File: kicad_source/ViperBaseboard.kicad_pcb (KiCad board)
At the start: 2 copper layers, 100 x 100 mm, 9 parts, among them CN1 ARDUINO_MKR, U1 VL53L0X, U2 VL53L0X, U3 VL53L0X, U4 VL53L0X

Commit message: updated layout, added step of baseboard
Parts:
- added U5: ublox_SAM-M8Q, RF_GPS:ublox_SAM-M8Q, B.Cu at (88.0, 87.0)
- added U6: BNO085, LGA:LGA-28-5832, F.Cu at (128.0, 87.0)
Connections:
- CN1 pad 22: (no net) -> SER_RX
- CN1 pad 23: (no net) -> SER_TX

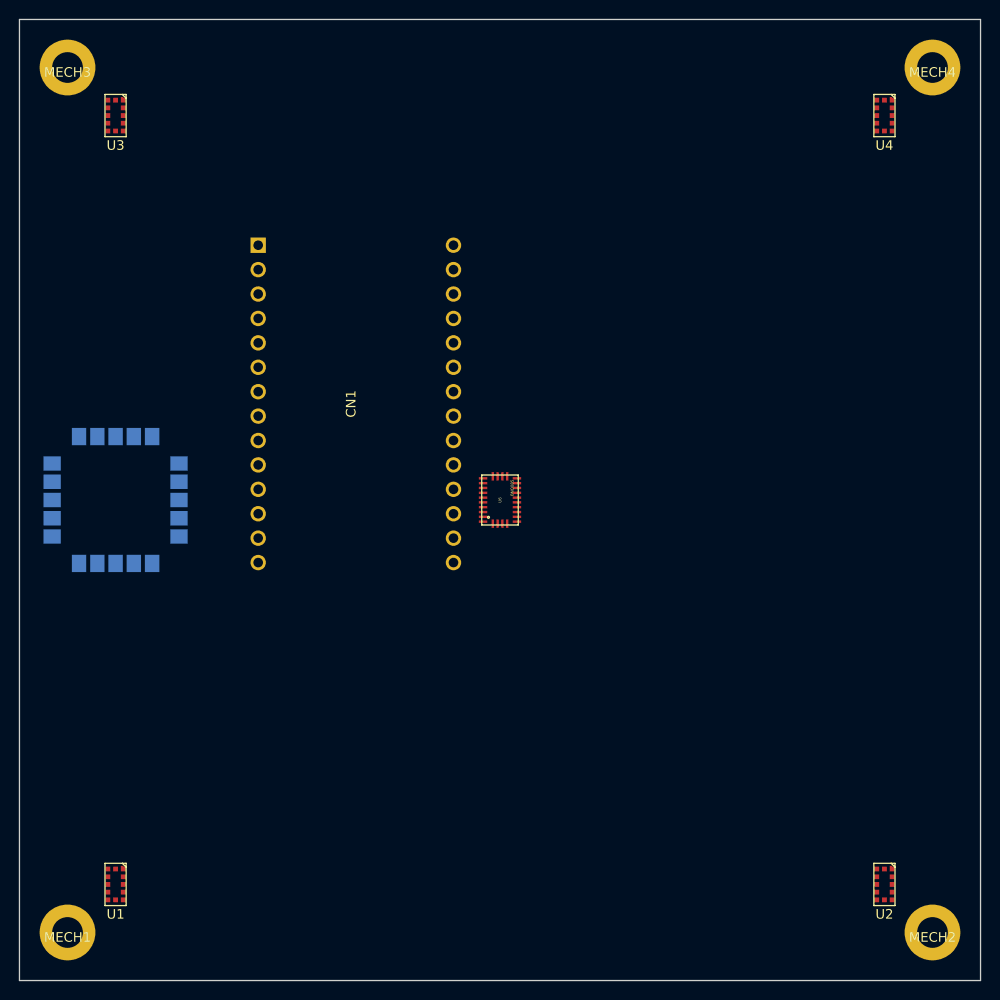
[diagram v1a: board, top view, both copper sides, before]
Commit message: redefined shape of PCB
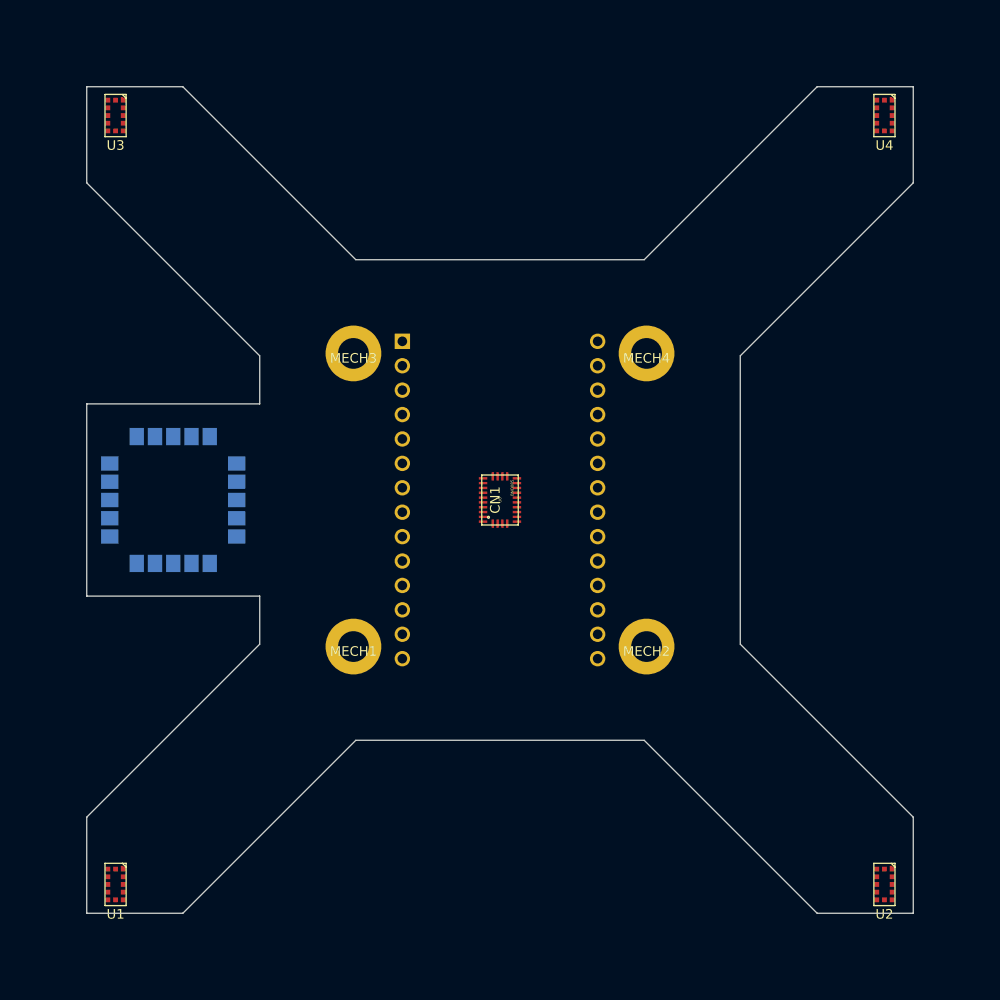
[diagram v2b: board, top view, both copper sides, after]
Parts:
- CN1: footprint MODULE_compute:ARDUINO_MKR -> MODULE_compute:ARDUINO_MKR_BASEBOARD
- moved MECH1 42.1 mm to (112.8, 102.2)
- moved MECH2 42.1 mm to (143.2, 102.2)
- moved MECH3 42.1 mm to (112.8, 71.8)
- moved MECH4 42.1 mm to (143.2, 71.8)
- moved CN1 18.0 mm to (128.0, 87.0)
- moved U5 6.00 mm to (94.0, 87.0)
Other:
- board size 100 x 100 mm -> 86 x 86 mm

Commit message: added BMP388
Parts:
- added C1: 100nF, capacitors:C_0603, F.Cu at (125.5, 78.2)
- added C2: 100nF, capacitors:C_0603, F.Cu at (125.5, 80.7)
- added U7: BMP388, IC_sensor:BMP388, F.Cu at (129.3, 78.7)

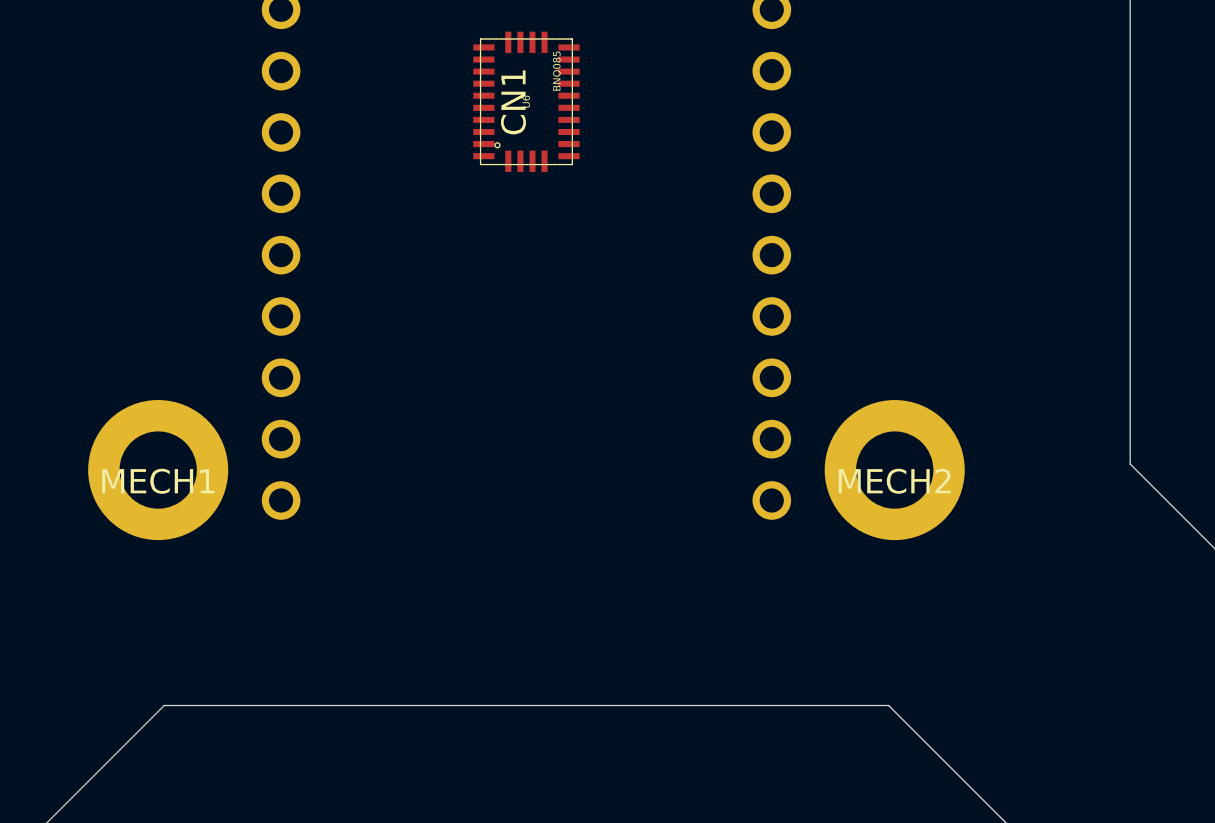
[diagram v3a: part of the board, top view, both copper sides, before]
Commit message: added schematic sheet with MCP2515
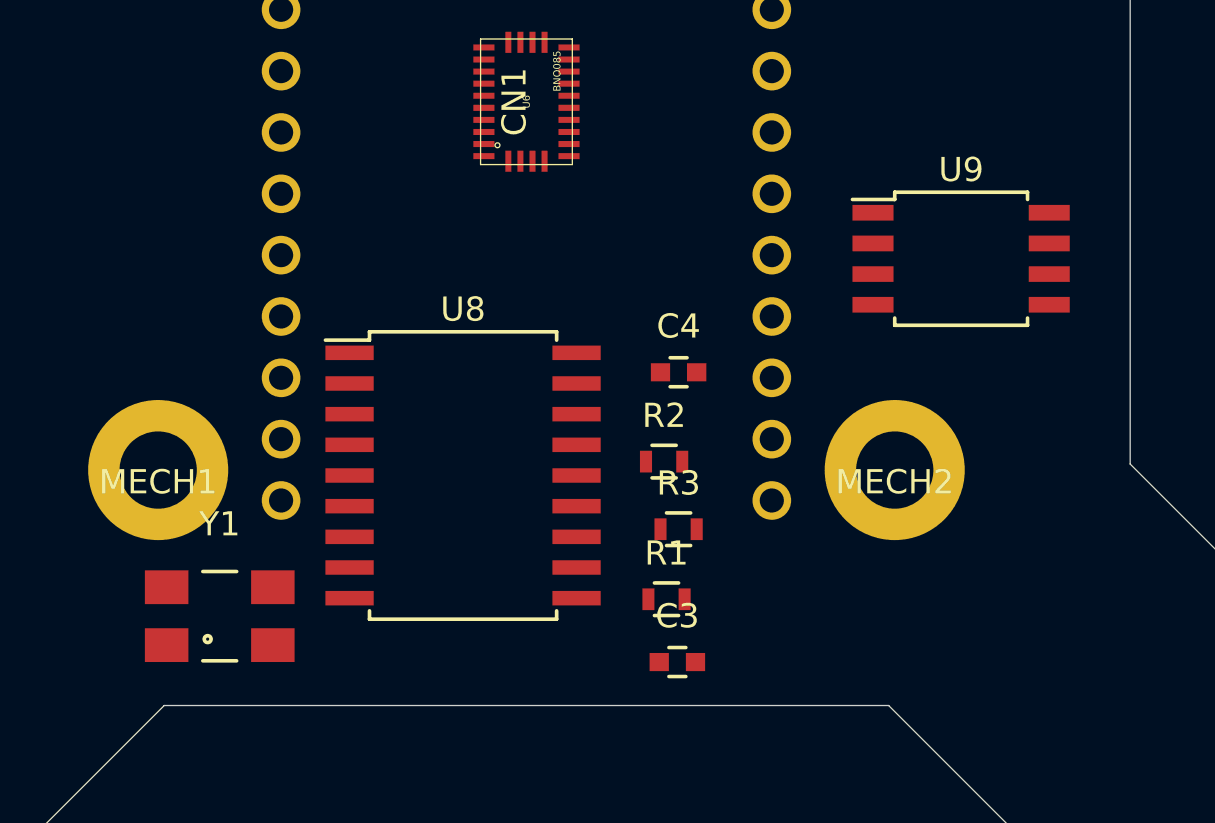
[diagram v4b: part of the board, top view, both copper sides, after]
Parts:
- added C3: 100nF, capacitors:C_0603, F.Cu at (134.2, 110.2)
- added C4: 100nF, capacitors:C_0603, F.Cu at (134.3, 98.2)
- added R1: 10k, resistors:R_0603, F.Cu at (133.8, 107.6)
- added R2: 10k, resistors:R_0603, F.Cu at (133.7, 101.9)
- added R3: 10k, resistors:R_0603, F.Cu at (134.3, 104.7)
- added U8: MCP2515, SOIC:SOIC-18_7.5x11.6mm_Pitch1.27mm, F.Cu at (125.4, 102.5)
- added U9: SN65HVD232, SOIC:SOIJ-8_5.3x5.3mm_Pitch1.27mm, F.Cu at (146.0, 93.5)
- added Y1: 16MHz, crystals:Crystal_SMD_0603_4Pads, F.Cu at (115.3, 108.3)
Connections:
- CN1 pad 12: (no net) -> MCP2515_CS
- CN1 pad 16: (no net) -> MCP2515_INT
- CN1 pad 17: (no net) -> MOSI
- CN1 pad 18: (no net) -> SCK
- CN1 pad 19: (no net) -> MISO

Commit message: added schematic sheet with sd-card
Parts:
- added C5: 100n, capacitors:C_0603, F.Cu at (134.0, 80.3)
- added CN2: Micro_SDCard, CON_wuerth:WE_693071010811, F.Cu at (135.1, 77.5)
- added R4: 100R, resistors:R_0603, F.Cu at (122.3, 79.6)
- added R5: 100R, resistors:R_0603, F.Cu at (123.9, 79.6)
- added R6: 100R, resistors:R_0603, F.Cu at (125.5, 79.6)
- added R7: 100R, resistors:R_0603, F.Cu at (129.6, 79.6)
- added R8: 10k, resistors:R_0603, F.Cu at (120.7, 79.6)
- moved U7 15.1 mm to (121.6, 91.7)
- moved C1 10.8 mm to (121.6, 88.3)
- moved C2 5.75 mm to (122.0, 85.3)
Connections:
- CN1 pad 13: (no net) -> SD_CS
